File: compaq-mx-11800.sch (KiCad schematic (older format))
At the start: 238 parts

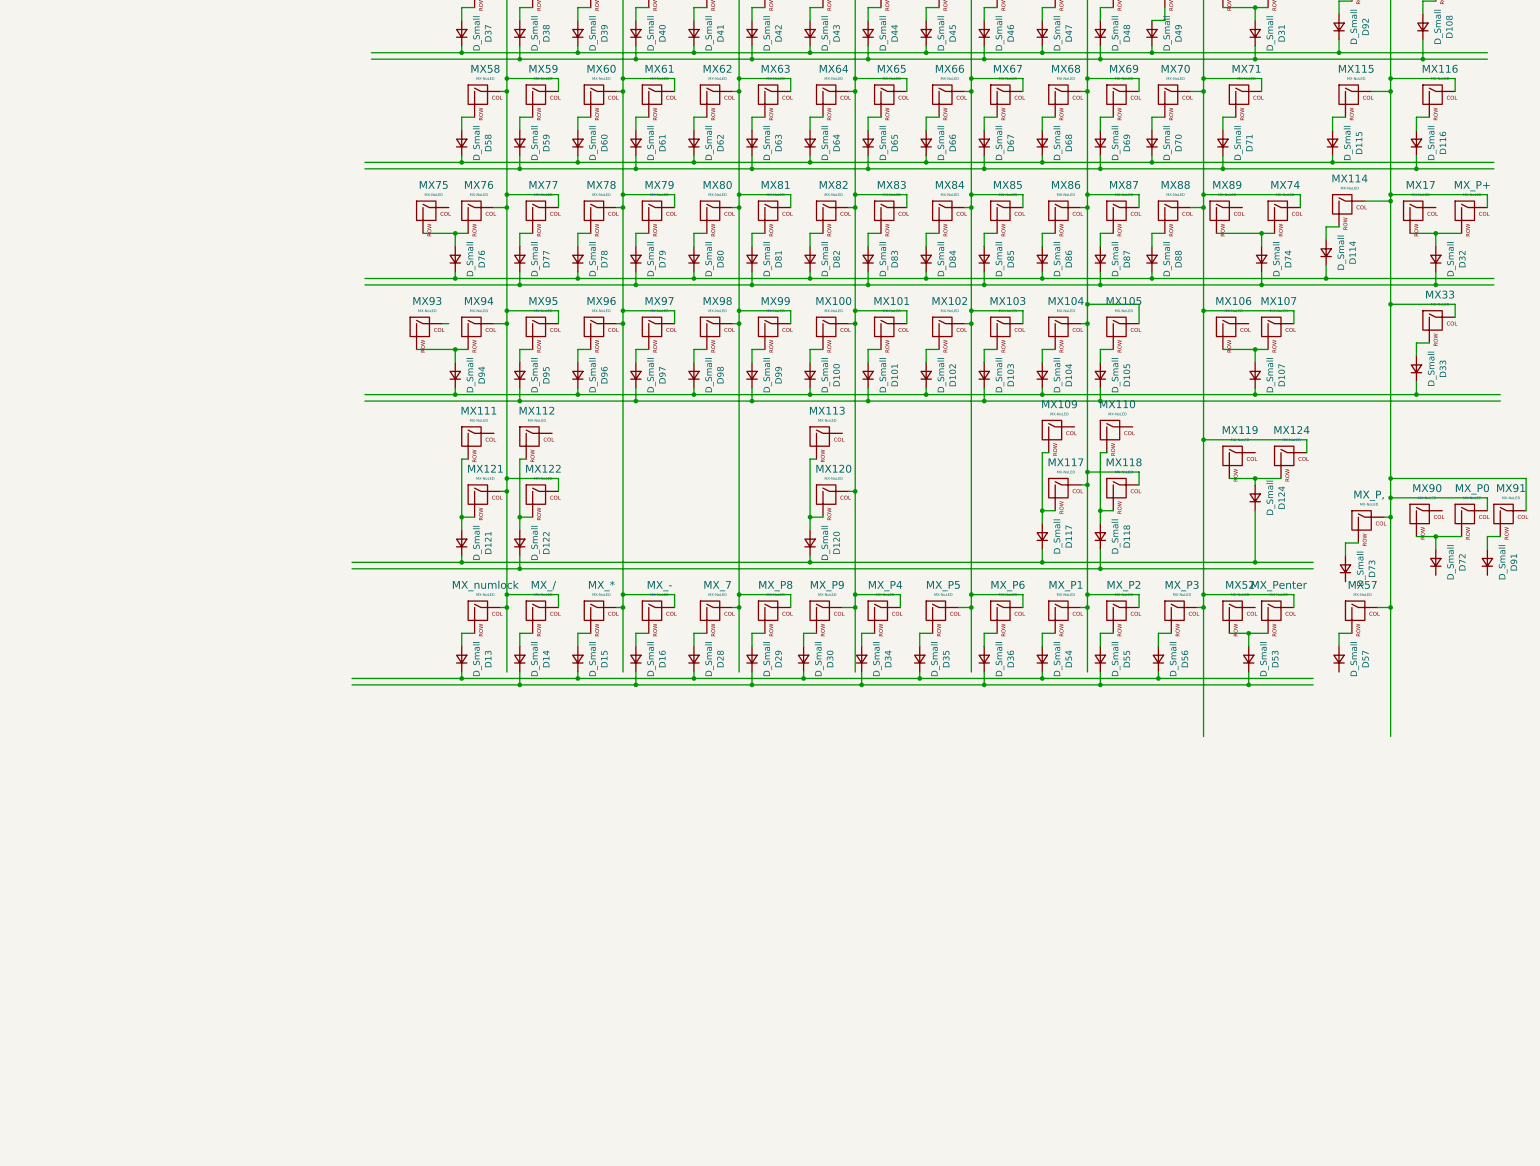
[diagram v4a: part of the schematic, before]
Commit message: rewire numpad in .sch
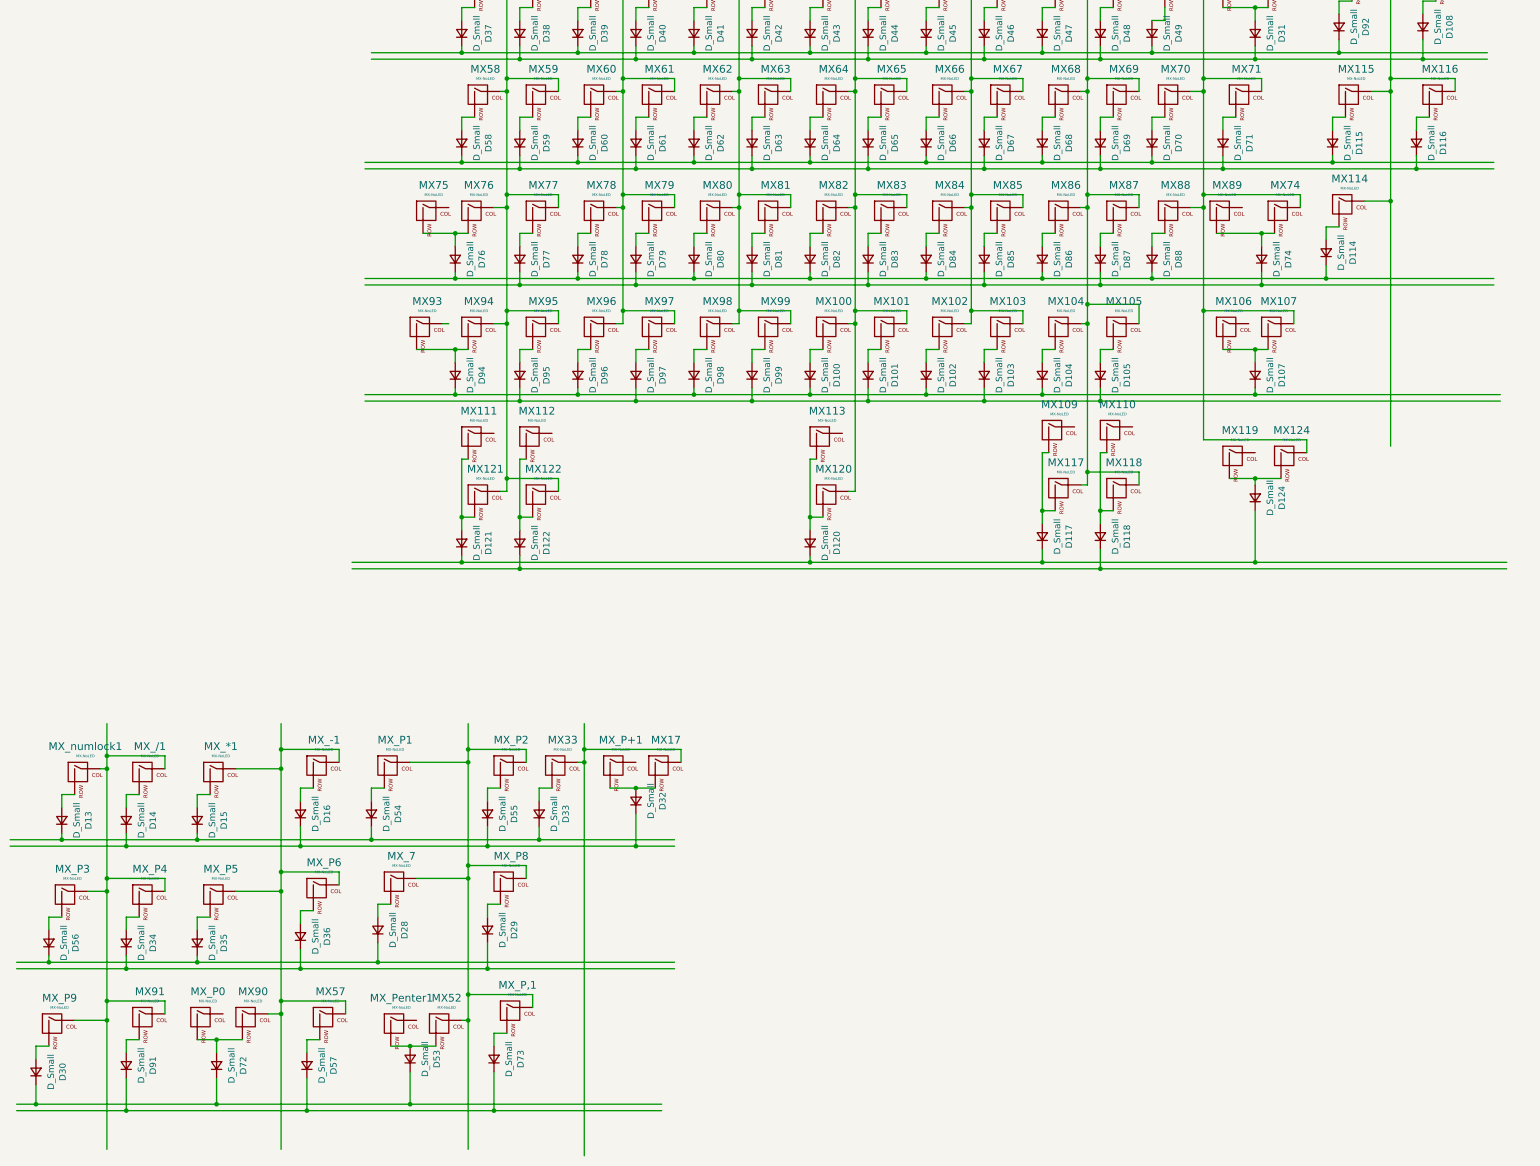
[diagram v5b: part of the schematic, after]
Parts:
- renumbered MX_* to MX_*1, MX_- to MX_-1, MX_/ to MX_/1, MX_P+ to MX_P+1, MX_P, to MX_P,1, MX_Penter to MX_Penter1, MX_numlock to MX_numlock1
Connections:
- wire segments 723 -> 729
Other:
- moved on the sheet: D13, D14, D15, D16, D28, D29, D30, D32, D33, D34, D35, D36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

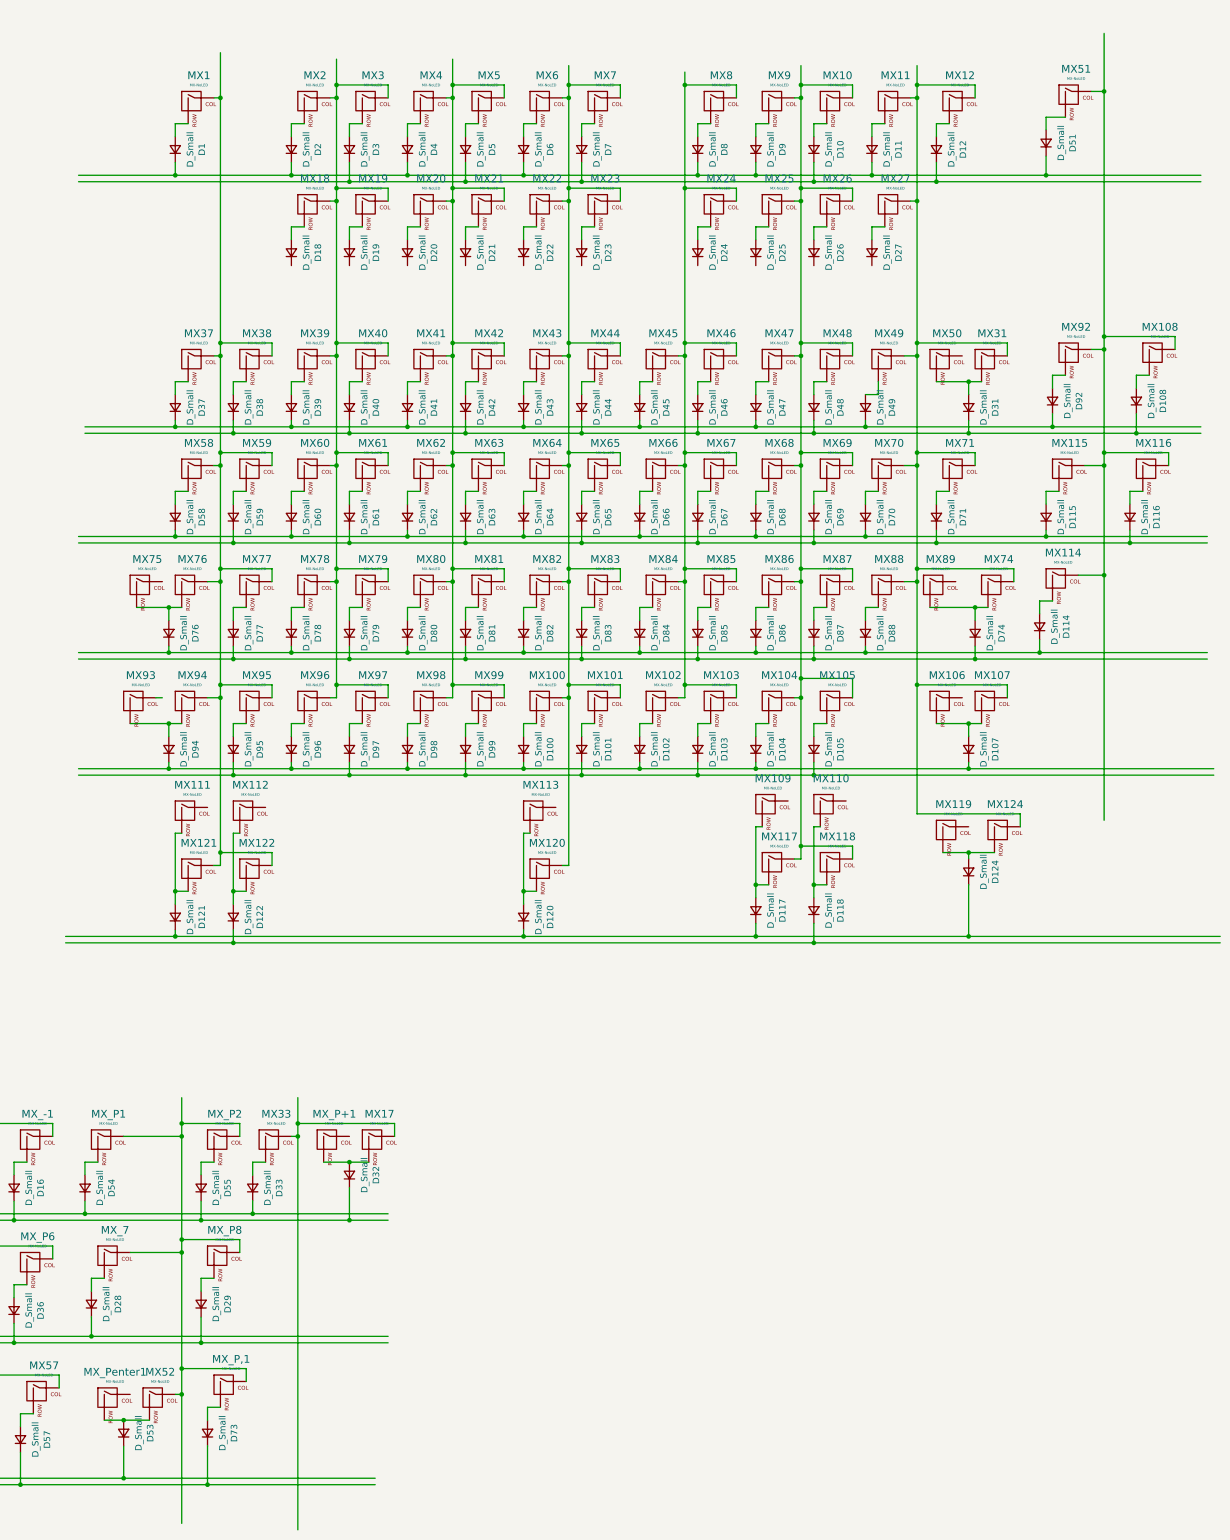
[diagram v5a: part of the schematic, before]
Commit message: connect the traces - numpad
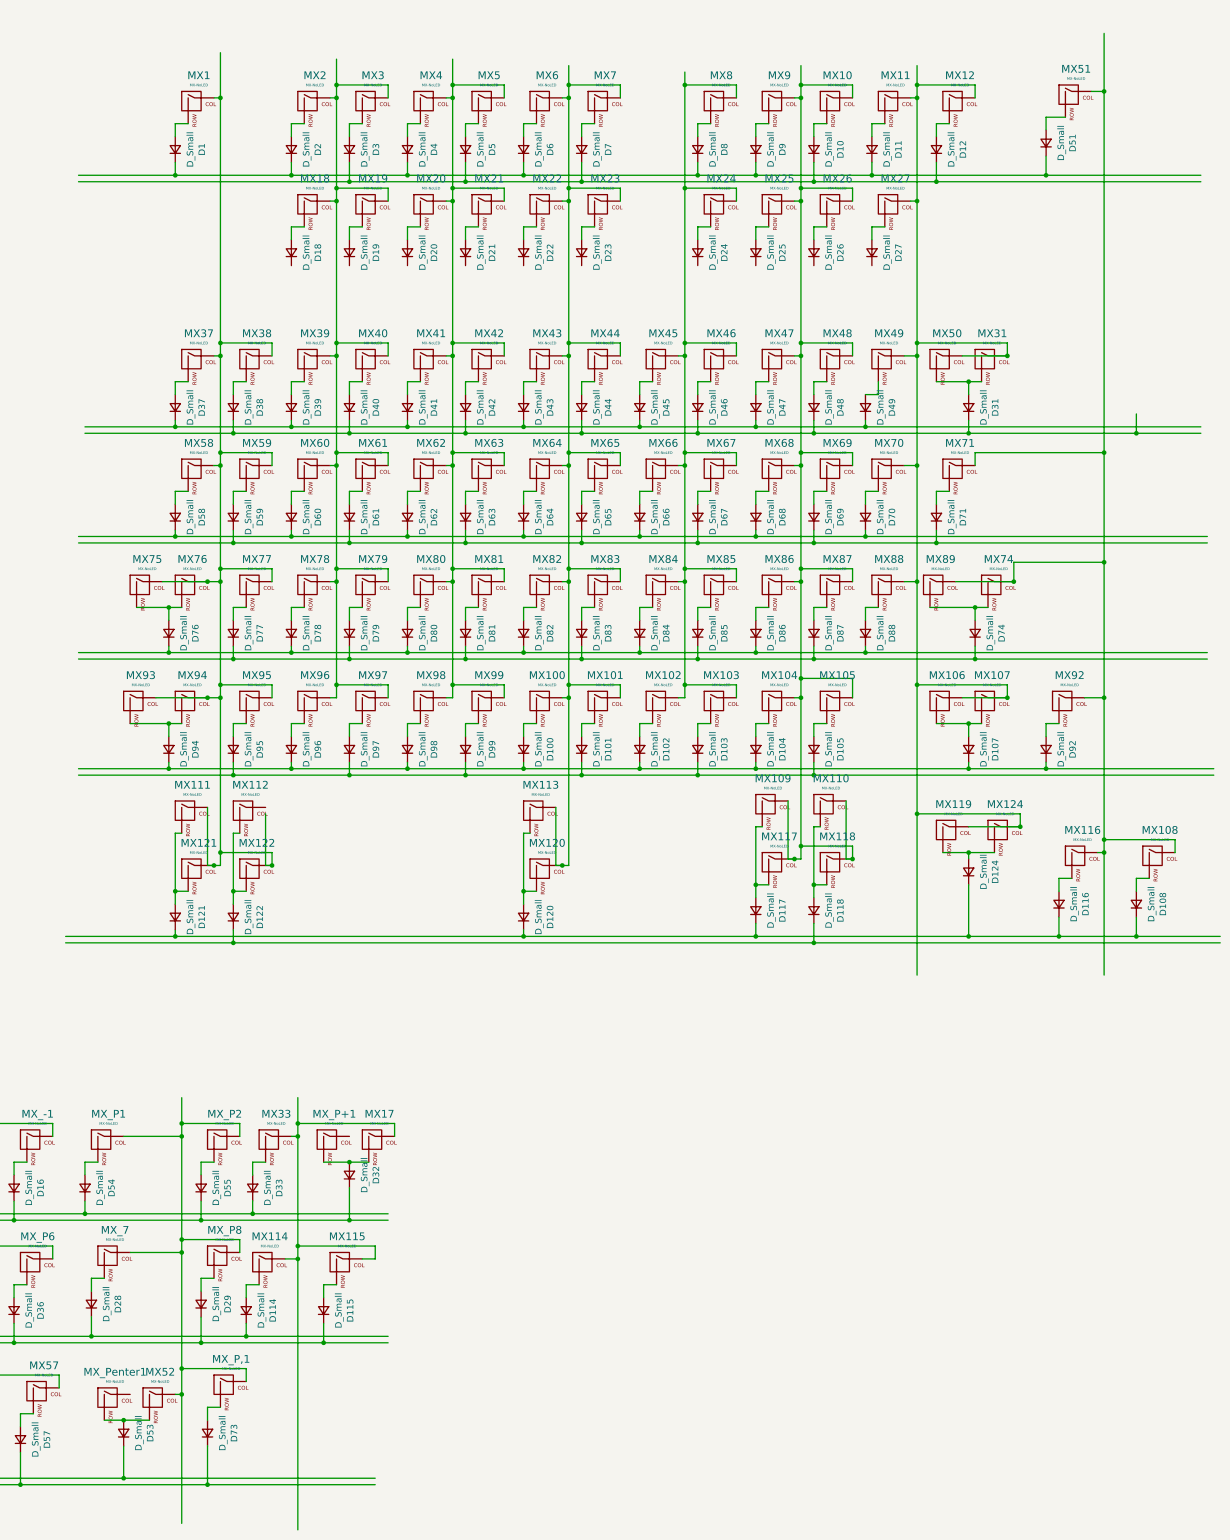
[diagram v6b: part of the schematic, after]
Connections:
- wire segments 729 -> 748
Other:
- moved on the sheet: D108, D114, D115, D116, D92, MX108, MX114, MX115, MX116, MX92
